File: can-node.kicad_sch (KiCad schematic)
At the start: 32 parts, among them J1 Conn_01x02_Pin, J2 Conn_01x02_Pin, J3 RJ45, J4 RJ45, J5 Conn_01x04_Pin, J6 Conn_01x04_Pin, J7 Screw_Terminal_01x02, SW1 SW_DIP_x04, SW2 SW_MEC_5G, SW3 SW_MEC_5G, U1 ESP32-S3, U2 MPU-9250, U3 MCP2551-I-SN

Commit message: v1 for esp32 breakout
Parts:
- removed C1, C2: 1 pF, Capacitor_SMD:C_0805_2012Metric_Pad1.18x1.45mm_HandSolder, symbol Device:C
- removed C4: 0.1 uF, Capacitor_SMD:C_0805_2012Metric_Pad1.18x1.45mm_HandSolder, symbol Device:C
- removed J5: Conn_01x04_Pin, Connector_PinHeader_1.00mm:PinHeader_1x04_P1.00mm_Horizontal, symbol Connector:Conn_01x04_Pin
- removed J7: Screw_Terminal_01x02, TerminalBlock:TerminalBlock_Altech_AK300-2_P5.00mm, symbol Connector:Screw_Terminal_01x02
- removed SW2, SW3: SW_MEC_5G, SMD_Buttons:SW_MEC_5GSH9, symbol Switch:SW_MEC_5G
- removed U1: ESP32-S3, Package_DFN_QFN:QFN-56-1EP_7x7mm_P0.4mm_EP5.6x5.6mm, symbol PCM_Espressif:ESP32-S3
- removed U2: MPU-9250, Sensor_Motion:InvenSense_QFN-24_3x3mm_P0.4mm, symbol Sensor_Motion:MPU-9250
- removed U3: MCP2551-I-SN, Package_SO:SOIC-8_3.9x4.9mm_P1.27mm, symbol Interface_CAN_LIN:MCP2551-I-SN
- removed U4: ~, md13:MD13S, symbol MD13S:MD13S
- added D3, D4, D5, D6: LED, LED_SMD:LED_0805_2012Metric_Pad1.15x1.40mm_HandSolder, symbol Device:LED
- added J10: Conn_01x06_Pin, Connector_PinHeader_1.00mm:PinHeader_1x06_P1.00mm_Vertical, symbol Connector:Conn_01x06_Pin
- added J11, J12, J13, J14, J8, J9: Conn_01x01_Socket, Connector_Wire:SolderWire-0.1sqmm_1x01_D0.4mm_OD1mm, symbol Connector:Conn_01x01_Socket
- added J15, J16, J17: Conn_01x01_Socket, Connector_Wire:SolderWire-0.5sqmm_1x01_D0.9mm_OD2.1mm, symbol Connector:Conn_01x01_Socket
- added J18, J19, J20, J21: Conn_01x01_Socket, Connector_Wire:SolderWire-2.5sqmm_1x01_D2.4mm_OD4.4mm, symbol Connector:Conn_01x01_Socket
- added J5: Conn_01x10_Pin, Connector_PinHeader_1.00mm:PinHeader_1x10_P1.00mm_Vertical, symbol Connector:Conn_01x10_Pin
- added J7: Conn_01x02_Pin, Connector_AMASS:AMASS_XT30U-F_1x02_P5.0mm_Vertical, symbol Connector:Conn_01x02_Pin
- added U1: ESP32-DEVKIT-V1, esp32:MODULE_ESP32_DEVKIT_V1, symbol ESP32-DEVKIT-V1:ESP32-DEVKIT-V1
- added U2: ~, MINI_360_Buck:MINI_360_Buck, symbol MINI360-buck:MINI360_Buck
- C3: value 1 pF -> 10 uF; footprint Capacitor_SMD:C_0805_2012Metric_Pad1.18x1.45mm_HandSolder -> Capacitor_SMD:C_0805_2012Metric
- R10, R9: value 1k -> 2k
- R3: value 60 -> 2k
- R4, R5, R6, R7: value 1k -> 10k
- R8: value 499 -> 2k
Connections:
- net +12 V: now also J20.1 (Pin_1), U2.1 (V_IN)
- net +3.3V: now also U1.1 (3V3), U1.16 (EN); no longer J3.3, J3.6, J4.1, J4.2, R10.1, R9.2
- net +5V: now also J5.10 (Pin_10), U1.30 (VIN), U2.3 (V_OUT); no longer J3.4, J3.5, J4.4, J4.5
- net ADD0: now also U1.14 (D22)
- net ADD1: now also U1.15 (D23)
- net ADD2: now also U1.23 (D25)
- net ADD3: now also U1.24 (D26)
- net CAN-Rx: now also J10.4 (Pin_4), U1.28 (D13)
- net CAN-Tx: now also J10.3 (Pin_3), U1.26 (D14)
- net DIR: now also J16.1 (Pin_1), U1.21 (D32)
- net ENC-A: now also J6.3 (Pin_3), U1.20 (D35); no longer J6.2 (Pin_2)
- net ENC-B: now also J6.4 (Pin_4), U1.19 (D34); no longer J6.3 (Pin_3)
- net GND: now also J4.1, J4.2, J6.2 (Pin_2), D3.1 (K), D4.1 (K), D5.1 (K), D6.1 (K), J10.2 (Pin_2), J15.1 (Pin_1), J21.1 (Pin_1), J5.9 (Pin_9), U1.2 (GND), U1.29 (GND), U2.2 (GND), U2.4 (GND); no longer J4.3, J4.6, J6.4 (Pin_4)
- net I2C-SCL: now also J5.8 (Pin_8), U1.10 (D19)
- net I2C-SDA: now also J5.7 (Pin_7), U1.11 (D21)
- net PWM: now also J17.1 (Pin_1), U1.25 (D27)
- net STATUS: now also U1.22 (D33)
- net LED3: now reaches R10.2
- net LED3: now also U1.27 (D12)
- net at R9.1: now also D5.2 (A)
- net at R8.1: now also D4.2 (A)
- net CAN_N renamed CAN-
- net CAN-: now also J10.6 (Pin_6), J12.1 (Pin_1), J14.1 (Pin_1), J9.1 (Pin_1); no longer R3.2
- net CAN_P renamed CAN+
- net CAN+: now also J10.5 (Pin_5), J11.1 (Pin_1), J13.1 (Pin_1), J8.1 (Pin_1); no longer R3.1
- net UART-Tx renamed LED1
- net LED1: now also U1.5 (D4)
- new net: D6.2 (A), R10.1
- new net: D3.2 (A), R3.1
- new net +5VA: J10.1 (Pin_1)
- new net FSYNC: J5.1 (Pin_1), U1.9 (D18)
- new net INT: J5.3 (Pin_3), U1.3 (D15)
- new net LED0: R3.2, U1.4 (D2)
- new net LED2: R9.2, U1.8 (D5)
- new net MOTOR_A: J18.1 (Pin_1), J7.2 (Pin_2)
- new net MOTOR_B: J19.1 (Pin_1), J7.1 (Pin_1)
- no-connect marks 44 -> 18
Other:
- note added: "12V to 5V Buck"
- note added: "AD0"
- note added: "Address Select"
- note added: "CAN Debug"
- note added: "CAN Termination"
- note added: "ECL"
- note added: "EDA"
- note added: "ESP32"
- note added: "Encoder Header"
- note added: "I2C Debug"
- note added: "I2C Pull-up"
- note added: "LEDs"
- note added: "MCP2551 CAN Transciever"
- note added: "MD13S"
- note added: "MPU9250 IMU"
- note added: "NCS"
- note added: "RJ-45 Connection"
- note added: "XT60 Power"
- moved on the sheet: J1, J2, J3, J4, J6, R1, R2, R4, R5, R6, R7, SW1

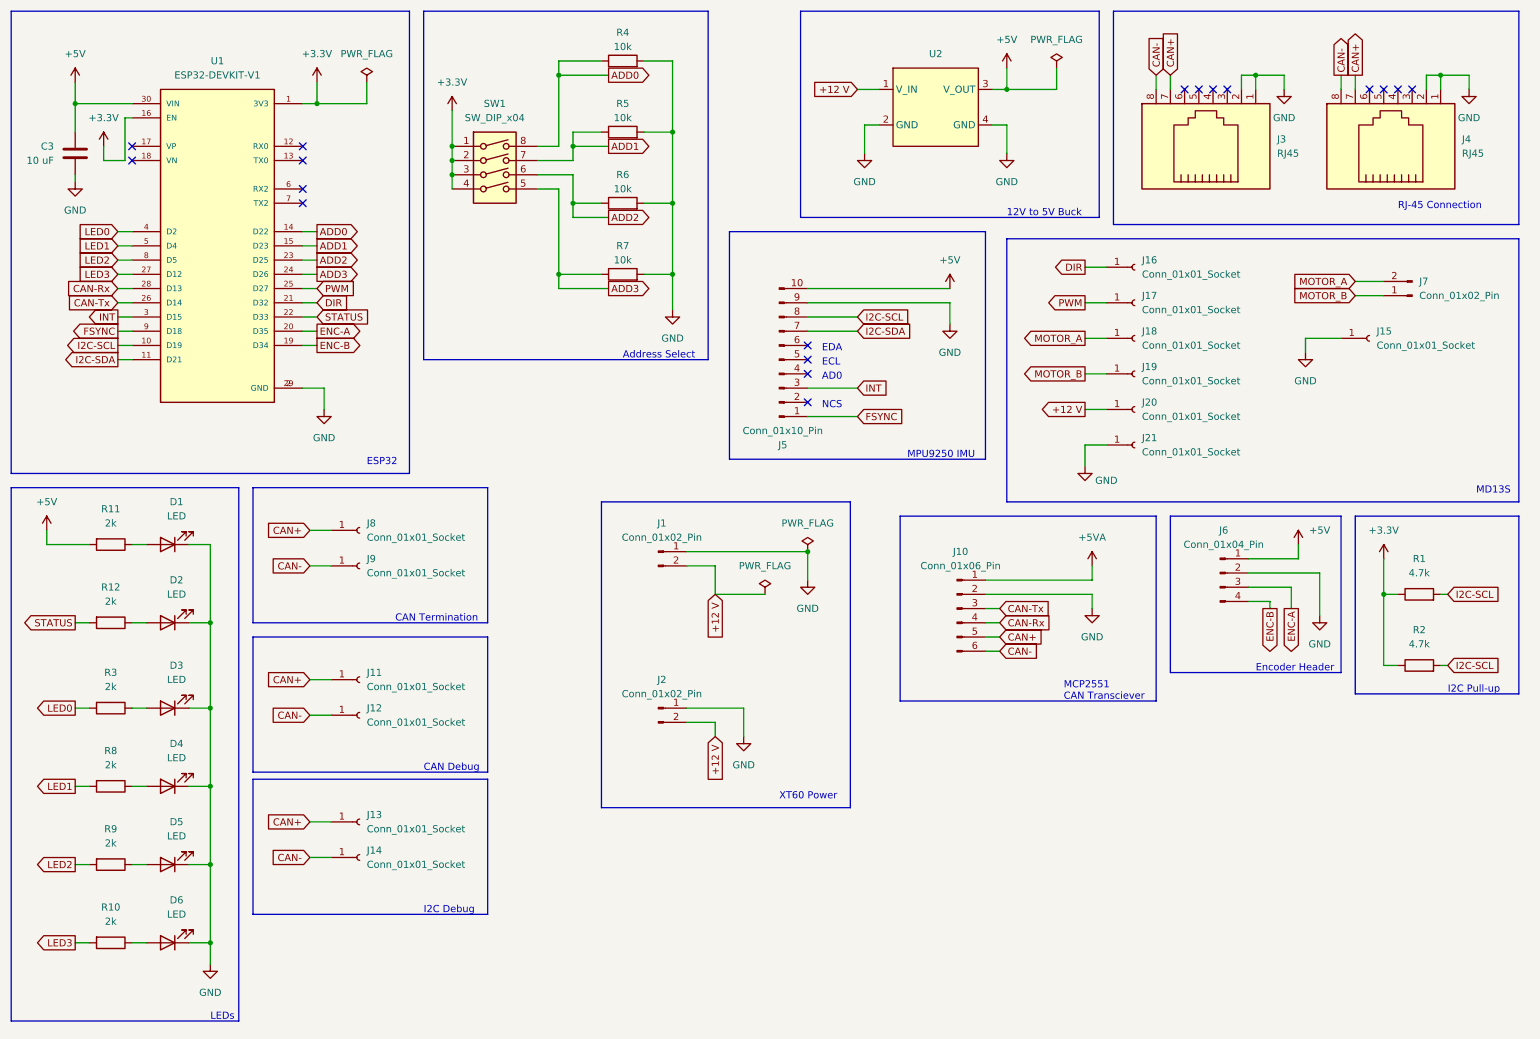
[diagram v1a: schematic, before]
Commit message: placed PCB components
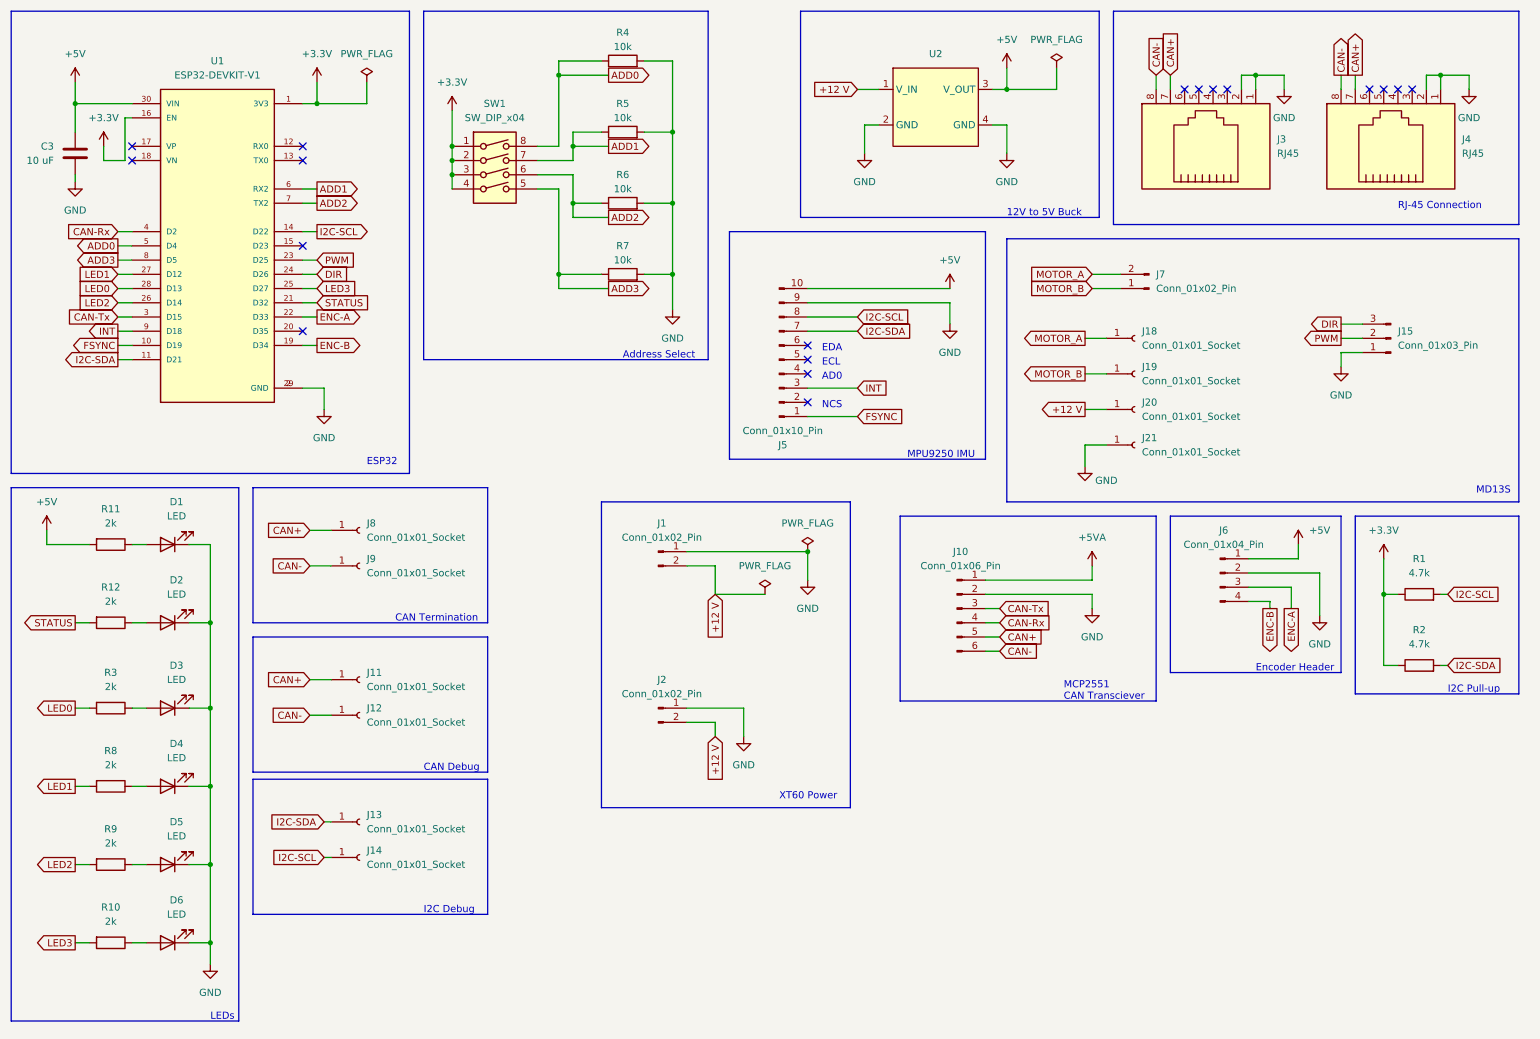
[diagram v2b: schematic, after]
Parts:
- removed J15, J16, J17: Conn_01x01_Socket, Connector_Wire:SolderWire-0.5sqmm_1x01_D0.9mm_OD2.1mm, symbol Connector:Conn_01x01_Socket
- added J15: Conn_01x03_Pin, Connector_JST:JST_EH_B3B-EH-A_1x03_P2.50mm_Vertical, symbol Connector:Conn_01x03_Pin
- J1: footprint Connector_AMASS:AMASS_XT60-F_1x02_P7.20mm_Vertical -> Connector_AMASS:AMASS_XT60PW-M_1x02_P7.20mm_Horizontal
- J10: footprint Connector_PinHeader_1.00mm:PinHeader_1x06_P1.00mm_Vertical -> Connector_PinHeader_2.00mm:PinHeader_1x06_P2.00mm_Vertical
- J2: footprint Connector_AMASS:AMASS_XT60-M_1x02_P7.20mm_Vertical -> Connector_AMASS:AMASS_XT60PW-M_1x02_P7.20mm_Horizontal
- J5: footprint Connector_PinHeader_1.00mm:PinHeader_1x10_P1.00mm_Vertical -> Connector_PinHeader_2.00mm:PinHeader_1x10_P2.00mm_Vertical
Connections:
- net ADD0: now also U1.5 (D4); no longer U1.14 (D22)
- net ADD1: now also U1.6 (RX2); no longer U1.15 (D23)
- net ADD2: now also U1.7 (TX2); no longer U1.23 (D25)
- net ADD3: now also U1.8 (D5); no longer U1.24 (D26)
- net CAN+: no longer J13.1 (Pin_1)
- net CAN-: no longer J14.1 (Pin_1)
- net CAN-Rx: now also U1.4 (D2); no longer U1.28 (D13)
- net CAN-Tx: now also U1.3 (D15); no longer U1.26 (D14)
- net DIR: now also U1.24 (D26), J15.3 (Pin_3); no longer U1.21 (D32)
- net ENC-A: now also U1.22 (D33); no longer U1.20 (D35)
- net FSYNC: now also U1.10 (D19); no longer U1.9 (D18)
- net GND: now also J15.1 (Pin_1)
- net I2C-SCL: now also J14.1 (Pin_1), U1.14 (D22); no longer R2.2, U1.10 (D19)
- net I2C-SDA: now also J13.1 (Pin_1), R2.2
- net INT: now also U1.9 (D18); no longer U1.3 (D15)
- net LED0: now also U1.28 (D13); no longer U1.4 (D2)
- net LED1: now also U1.27 (D12); no longer U1.5 (D4)
- net LED2: now also U1.26 (D14); no longer U1.8 (D5)
- net LED3: now also U1.25 (D27); no longer U1.27 (D12)
- net PWM: now also U1.23 (D25), J15.2 (Pin_2); no longer U1.25 (D27)
- net STATUS: now also U1.21 (D32); no longer U1.22 (D33)
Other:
- moved on the sheet: J7

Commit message: draft?
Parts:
- removed J11, J12: Conn_01x01_Socket, Connector_Wire:SolderWire-0.1sqmm_1x01_D0.4mm_OD1mm, symbol Connector:Conn_01x01_Socket
- removed J18, J19, J20, J21: Conn_01x01_Socket, Connector_Wire:SolderWire-2.5sqmm_1x01_D2.4mm_OD4.4mm, symbol Connector:Conn_01x01_Socket
- added J16, J17: Conn_01x02_Pin, Connector_Wire:SolderWire-1sqmm_1x02_P5.4mm_D1.4mm_OD2.7mm, symbol Connector:Conn_01x02_Pin
- added R13: 60, Resistor_THT:R_Axial_DIN0207_L6.3mm_D2.5mm_P10.16mm_Horizontal, symbol Device:R
- D1, D2, D3, D4, D5, D6: footprint LED_SMD:LED_0805_2012Metric_Pad1.15x1.40mm_HandSolder -> LED_THT:LED_D3.0mm
- J1, J2: footprint Connector_AMASS:AMASS_XT60PW-M_1x02_P7.20mm_Horizontal -> Connector_Wire:SolderWire-1.5sqmm_1x02_P7.8mm_D1.7mm_OD3.9mm
- J7: footprint Connector_AMASS:AMASS_XT30U-F_1x02_P5.0mm_Vertical -> Connector_Wire:SolderWire-1.5sqmm_1x02_P7.8mm_D1.7mm_OD3.9mm
- R1, R10, R11, R12, R2, R3, R4, R5, R6, R7, R8, R9: footprint Resistor_SMD:R_0805_2012Metric_Pad1.20x1.40mm_HandSolder -> Resistor_THT:R_Axial_DIN0207_L6.3mm_D2.5mm_P10.16mm_Horizontal
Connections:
- net +12 V: now also J17.2 (Pin_2)
- net CAN+: now also R13.1; no longer J8.1 (Pin_1)
- net CAN-: now also R13.2; no longer J9.1 (Pin_1)
- net CAN-Rx: now also J8.1 (Pin_1)
- net CAN-Tx: now also J9.1 (Pin_1)
- net GND: now also J17.1 (Pin_1)
- net MOTOR_A: now also J16.2 (Pin_2)
- net MOTOR_B: now also J16.1 (Pin_1)

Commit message: first try
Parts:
- R1, R10, R11, R12, R13, R2, R3, R4, R5, R6, R7, R8, R9: footprint Resistor_THT:R_Axial_DIN0207_L6.3mm_D2.5mm_P10.16mm_Horizontal -> Resistor_THT:R_Axial_DIN0204_L3.6mm_D1.6mm_P5.08mm_Horizontal
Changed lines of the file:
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@@
       (effects (font (size 1.27 1.27)))
     )
-    (property "Footprint" "Resistor_THT:R_Axial_DIN0207_L6.3mm_D2.5mm_P10.16mm_Horizontal" (at 31.75 121.412 90)
+    (property "Footprint" "Resistor_THT:R_Axial_DIN0204_L3.6mm_D1.6mm_P5.08mm_Horizontal" (at 31.75 121.412 90)
       (effects (font (size 1.27 1.27)) hide)
     )
@@
       (effects (font (size 1.27 1.27)))
     )
-    (property "Footprint" "Resistor_THT:R_Axial_DIN0207_L6.3mm_D2.5mm_P10.16mm_Horizontal" (at 31.75 107.442 90)
+    (property "Footprint" "Resistor_THT:R_Axial_DIN0204_L3.6mm_D1.6mm_P5.08mm_Horizontal" (at 31.75 107.442 90)
       (effects (font (size 1.27 1.27)) hide)
     )
@@
       (effects (font (size 1.27 1.27)) (justify left))
     )
-    (property "Footprint" "Resistor_THT:R_Axial_DIN0207_L6.3mm_D2.5mm_P10.16mm_Horizontal" (at 84.582 137.16 90)
+    (property "Footprint" "Resistor_THT:R_Axial_DIN0204_L3.6mm_D1.6mm_P5.08mm_Horizontal" (at 84.582 137.16 90)
       (effects (font (size 1.27 1.27)) hide)
     )
@@
       (effects (font (size 1.27 1.27)))
     )
-    (property "Footprint" "Resistor_THT:R_Axial_DIN0207_L6.3mm_D2.5mm_P10.16mm_Horizontal" (at 265.43 119.888 90)
+    (property "Footprint" "Resistor_THT:R_Axial_DIN0204_L3.6mm_D1.6mm_P5.08mm_Horizontal" (at 265.43 119.888 90)
       (effects (font (size 1.27 1.27)) hide)
     )
@@
       (effects (font (size 1.27 1.27)))
     )
-    (property "Footprint" "Resistor_THT:R_Axial_DIN0207_L6.3mm_D2.5mm_P10.16mm_Horizontal" (at 123.19 50.038 90)
+    (property "Footprint" "Resistor_THT:R_Axial_DIN0204_L3.6mm_D1.6mm_P5.08mm_Horizontal" (at 123.19 50.038 90)
       (effects (font (size 1.27 1.27)) hide)
     )
@@
       (effects (font (size 1.27 1.27)))
     )
-    (property "Footprint" "Resistor_THT:R_Axial_DIN0207_L6.3mm_D2.5mm_P10.16mm_Horizontal" (at 31.75 164.592 90)
+    (property "Footprint" "Resistor_THT:R_Axial_DIN0204_L3.6mm_D1.6mm_P5.08mm_Horizontal" (at 31.75 164.592 90)
       (effects (font (size 1.27 1.27)) hide)
     )
@@
       (effects (font (size 1.27 1.27)))
     )
-    (property "Footprint" "Resistor_THT:R_Axial_DIN0207_L6.3mm_D2.5mm_P10.16mm_Horizontal" (at 123.19 24.638 90)
+    (property "Footprint" "Resistor_THT:R_Axial_DIN0204_L3.6mm_D1.6mm_P5.08mm_Horizontal" (at 123.19 24.638 90)
       (effects (font (size 1.27 1.27)) hide)
     )
@@
       (effects (font (size 1.27 1.27)))
     )
-    (property "Footprint" "Resistor_THT:R_Axial_DIN0207_L6.3mm_D2.5mm_P10.16mm_Horizontal" (at 123.19 37.338 90)
+    (property "Footprint" "Resistor_THT:R_Axial_DIN0204_L3.6mm_D1.6mm_P5.08mm_Horizontal" (at 123.19 37.338 90)
       (effects (font (size 1.27 1.27)) hide)
     )
@@
       (effects (font (size 1.27 1.27)))
     )
-    (property "Footprint" "Resistor_THT:R_Axial_DIN0207_L6.3mm_D2.5mm_P10.16mm_Horizontal" (at 123.19 62.738 90)
+    (property "Footprint" "Resistor_THT:R_Axial_DIN0204_L3.6mm_D1.6mm_P5.08mm_Horizontal" (at 123.19 62.738 90)
       (effects (font (size 1.27 1.27)) hide)
     )
@@
       (effects (font (size 1.27 1.27)))
     )
-    (property "Footprint" "Resistor_THT:R_Axial_DIN0207_L6.3mm_D2.5mm_P10.16mm_Horizontal" (at 31.75 150.622 90)
+    (property "Footprint" "Resistor_THT:R_Axial_DIN0204_L3.6mm_D1.6mm_P5.08mm_Horizontal" (at 31.75 150.622 90)
       (effects (font (size 1.27 1.27)) hide)
     )
@@
       (effects (font (size 1.27 1.27)))
     )
-    (property "Footprint" "Resistor_THT:R_Axial_DIN0207_L6.3mm_D2.5mm_P10.16mm_Horizontal" (at 265.43 132.588 90)
+    (property "Footprint" "Resistor_THT:R_Axial_DIN0204_L3.6mm_D1.6mm_P5.08mm_Horizontal" (at 265.43 132.588 90)
       (effects (font (size 1.27 1.27)) hide)
     )
@@
       (effects (font (size 1.27 1.27)))
     )
-    (property "Footprint" "Resistor_THT:R_Axial_DIN0207_L6.3mm_D2.5mm_P10.16mm_Horizontal" (at 31.75 178.562 90)
+    (property "Footprint" "Resistor_THT:R_Axial_DIN0204_L3.6mm_D1.6mm_P5.08mm_Horizontal" (at 31.75 178.562 90)
       (effects (font (size 1.27 1.27)) hide)
     )
@@
       (effects (font (size 1.27 1.27)))
     )
-    (property "Footprint" "Resistor_THT:R_Axial_DIN0207_L6.3mm_D2.5mm_P10.16mm_Horizontal" (at 31.75 136.652 90)
-      (effects (font (size 1.27 1.27)) hide)
-    )
+    (property "Footprint" "Resistor_THT:R_Axial_DIN0204_L3.6mm_D1.6mm_P5.08mm_Horizontal" (at 31.75 136.652 90)
+      (effects (font (size 1.27 1.27)) hide)
+    )

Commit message: fixed footprints
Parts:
- J10: footprint Connector_PinHeader_2.00mm:PinHeader_1x06_P2.00mm_Vertical -> Connector_PinHeader_2.54mm:PinHeader_1x06_P2.54mm_Vertical
- J15: footprint Connector_JST:JST_EH_B3B-EH-A_1x03_P2.50mm_Vertical -> Connector_JST:JST_PH_B3B-PH-K_1x03_P2.00mm_Vertical
- J5: footprint Connector_PinHeader_2.00mm:PinHeader_1x10_P2.00mm_Vertical -> Connector_PinHeader_2.54mm:PinHeader_1x10_P2.54mm_Vertical
- J6: footprint Connector_JST:JST_EH_S4B-EH_1x04_P2.50mm_Horizontal -> Connector_JST:JST_PH_B4B-PH-K_1x04_P2.00mm_Vertical
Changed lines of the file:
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@@
       (effects (font (size 1.27 1.27)))
     )
-    (property "Footprint" "Connector_PinHeader_2.00mm:PinHeader_1x06_P2.00mm_Vertical" (at 182.88 120.65 0)
+    (property "Footprint" "Connector_PinHeader_2.54mm:PinHeader_1x06_P2.54mm_Vertical" (at 182.88 120.65 0)
       (effects (font (size 1.27 1.27)) hide)
     )
@@
       (effects (font (size 1.27 1.27)))
     )
-    (property "Footprint" "Connector_JST:JST_EH_S4B-EH_1x04_P2.50mm_Horizontal" (at 229.87 114.3 0)
+    (property "Footprint" "Connector_JST:JST_PH_B4B-PH-K_1x04_P2.00mm_Vertical" (at 229.87 114.3 0)
       (effects (font (size 1.27 1.27)) hide)
     )
@@
       (effects (font (size 1.27 1.27)) (justify right))
     )
-    (property "Footprint" "Connector_JST:JST_EH_B3B-EH-A_1x03_P2.50mm_Vertical" (at 260.35 72.39 0)
+    (property "Footprint" "Connector_JST:JST_PH_B3B-PH-K_1x03_P2.00mm_Vertical" (at 260.35 72.39 0)
       (effects (font (size 1.27 1.27)) hide)
     )
@@
       (effects (font (size 1.27 1.27)))
     )
-    (property "Footprint" "Connector_PinHeader_2.00mm:PinHeader_1x10_P2.00mm_Vertical" (at 151.13 76.2 0)
-      (effects (font (size 1.27 1.27)) hide)
-    )
+    (property "Footprint" "Connector_PinHeader_2.54mm:PinHeader_1x10_P2.54mm_Vertical" (at 151.13 76.2 0)
+      (effects (font (size 1.27 1.27)) hide)
+    )
